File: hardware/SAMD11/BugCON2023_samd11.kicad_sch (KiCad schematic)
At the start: 30 parts, among them J1 I2C, J3 PAD2, J4 PAD, J5 Serial, P1 USB_C_Plug_USB2.0, Q1 DMG3415U-7, SW1 SW_Push, SW2 ON, U1 ATSAMD11C14A-SS, U2 AP2112K-3.3

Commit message: change MCU for RP2040
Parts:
- removed SW1: SW_Push, Button_Switch_SMD:SW_SPST_TL3342, symbol Switch:SW_Push
- removed U1: ATSAMD11C14A-SS, Package_SO:SOIC-14_3.9x8.7mm_P1.27mm, symbol MCU_Microchip_SAMD:ATSAMD11C14A-SS
- added C10, C12, C14, C15, C16, C17, C18, C19, C20: 0.1uF, Capacitor_SMD:C_0402_1005Metric, symbol Device:C_Small
- added C11, C9: 27pF, Capacitor_SMD:C_0402_1005Metric, symbol Device:C_Small
- added C13, C8: 1uF, Capacitor_SMD:C_0402_1005Metric, symbol Device:C_Small
- added JP1: BOOT, Jumper:SolderJumper-2_P1.3mm_Open_TrianglePad1.0x1.5mm, symbol Jumper:Jumper_2_Open
- added R10: 10k, Resistor_SMD:R_0402_1005Metric, symbol Device:R_Small
- added R7, R8: 27, Resistor_SMD:R_0402_1005Metric, symbol Device:R_Small
- added R9: 1k, Resistor_SMD:R_0402_1005Metric, symbol Device:R_Small
- added RESET1: SW, CatSniffer:TS1088R02026, symbol CatSniffer-rescue:SW_Push-Switch-CatStick-rescue-CatSniffer-rescue
- added U1: W25Q16JV, CatSniffer:W25Q16JVUUIQ, symbol Memory_Flash:W25Q128JVS
- added U3: RP2040, Package_DFN_QFN:QFN-56-1EP_7x7mm_P0.4mm_EP3.2x3.2mm, symbol MCU_RaspberryPi:RP2040
- added Y1: 12MHz, Crystal:Crystal_SMD_3225-4Pin_3.2x2.5mm, symbol Device:Crystal_GND23_Small
- C1: value 100nF -> 0.1uF; footprint Capacitor_SMD:C_0603_1608Metric -> Capacitor_SMD:C_0402_1005Metric; LCSC# C1591 -> (none); Mouser# (none) -> 963-MSAST105SB7104KF; Proveedor LCSC -> (none); manf# CL10B104KB8NNNC -> MSAST105SB7104KFNB25; provedor (none) -> Mouser
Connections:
- net +3.3V: now also C13.1, C14.1, C15.1, C16.1, C17.1, C18.1, C19.1, C20.1, R10.1, U1.8 (VCC), U3.1 (IOVDD), U3.10 (IOVDD), U3.22 (IOVDD), U3.33 (IOVDD), U3.42 (IOVDD), U3.43 (ADC_AVDD), U3.44 (VREG_IN), U3.48 (USB_VDD), U3.49 (IOVDD)
- net D+: now also R7.1
- net D-: now also R8.1
- net GND: now also C10.2, C11.2, C12.2, C13.2, C14.2, C15.2, C16.2, C17.2, C18.2, C19.2, C20.2, C8.2, C9.2, JP1.1 (A), RESET1.2, U1.4 (GND), U3.19 (TESTEN), U3.57 (GND), Y1.2, Y1.4
- net PIN: now also U3.35 (GPIO23)
- net RX: now also U3.12 (GPIO9)
- net SCL: now also U3.16 (GPIO13)
- net SDA: now also U3.15 (GPIO12)
- net TX: now also U3.11 (GPIO8)
- new net: C9.1, U3.20 (XIN), Y1.1
- new net: R9.2, U3.21 (XOUT)
- new net: R8.2, U3.46 (USB_DM)
- new net: R7.2, U3.47 (USB_DP)
- new net: C11.1, R9.1, Y1.3
- new net +1V2: C10.1, C12.1, C8.1, U3.23 (DVDD), U3.45 (VREG_VOUT), U3.50 (DVDD)
- new net QSPI_CS: JP1.2 (B)
- new net QSPI_SCK: U1.6 (CLK), U3.52 (QSPI_SCLK)
- new net QSPI_SD0: U1.5 (DI(IO0)), U3.53 (QSPI_SD0)
- new net QSPI_SD1: U1.2 (DO(IO1)), U3.55 (QSPI_SD1)
- new net QSPI_SD2: U1.3 (IO2), U3.54 (QSPI_SD2)
- new net QSPI_SD3: U1.7 (IO3), U3.51 (QSPI_SD3)
- new net QSPI_SS: R10.2, U1.1 (~{CS}), U3.56 (QSPI_SS)
- new net RESET: RESET1.1, U3.26 (RUN)
- no-connect marks 1 -> 28
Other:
- note added: "FLASH"
- note added: "MICROCONTROLLER"
- note removed: "Microcontroller"
- note removed: "RST"
- moved on the sheet: C4, C5, C6, C7, D2, D3, D4, D5, J3, J4, R4

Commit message: upd floorplan on rp2040 badge
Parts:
- RESET1: footprint CatSniffer:TS1088R02026 -> Button_Switch_SMD:SW_SPST_TL3342; LCSC# C455281 -> (none); manf# TS-1088R-02526 -> (none)
- U1: footprint CatSniffer:W25Q16JVUUIQ -> BugCON2023_samd11:W25Q16JVUUIQ
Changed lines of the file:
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@@
       (effects (font (size 1.27 1.27)))
     )
-    (property "Footprint" "CatSniffer:TS1088R02026" (at 188.468 147.955 0)
+    (property "Footprint" "Button_Switch_SMD:SW_SPST_TL3342" (at 188.468 147.955 0)
       (effects (font (size 1.27 1.27)) hide)
     )
@@
       (effects (font (size 1.27 1.27)) hide)
     )
-    (property "LCSC#" "C455281" (at 188.468 153.035 0)
+    (property "LCSC#" "" (at 188.468 153.035 0)
       (effects (font (size 1.27 1.27)) hide)
     )
-    (property "manf#" "TS-1088R-02526" (at 188.468 153.035 0)
+    (property "manf#" "" (at 188.468 153.035 0)
       (effects (font (size 1.27 1.27)) hide)
     )
@@
       (effects (font (size 1.27 1.27)) (justify left))
     )
-    (property "Footprint" "CatSniffer:W25Q16JVUUIQ" (at 81.661 252.603 0)
+    (property "Footprint" "BugCON2023_samd11:W25Q16JVUUIQ" (at 81.661 252.603 0)
       (effects (font (size 1.27 1.27)) hide)
     )

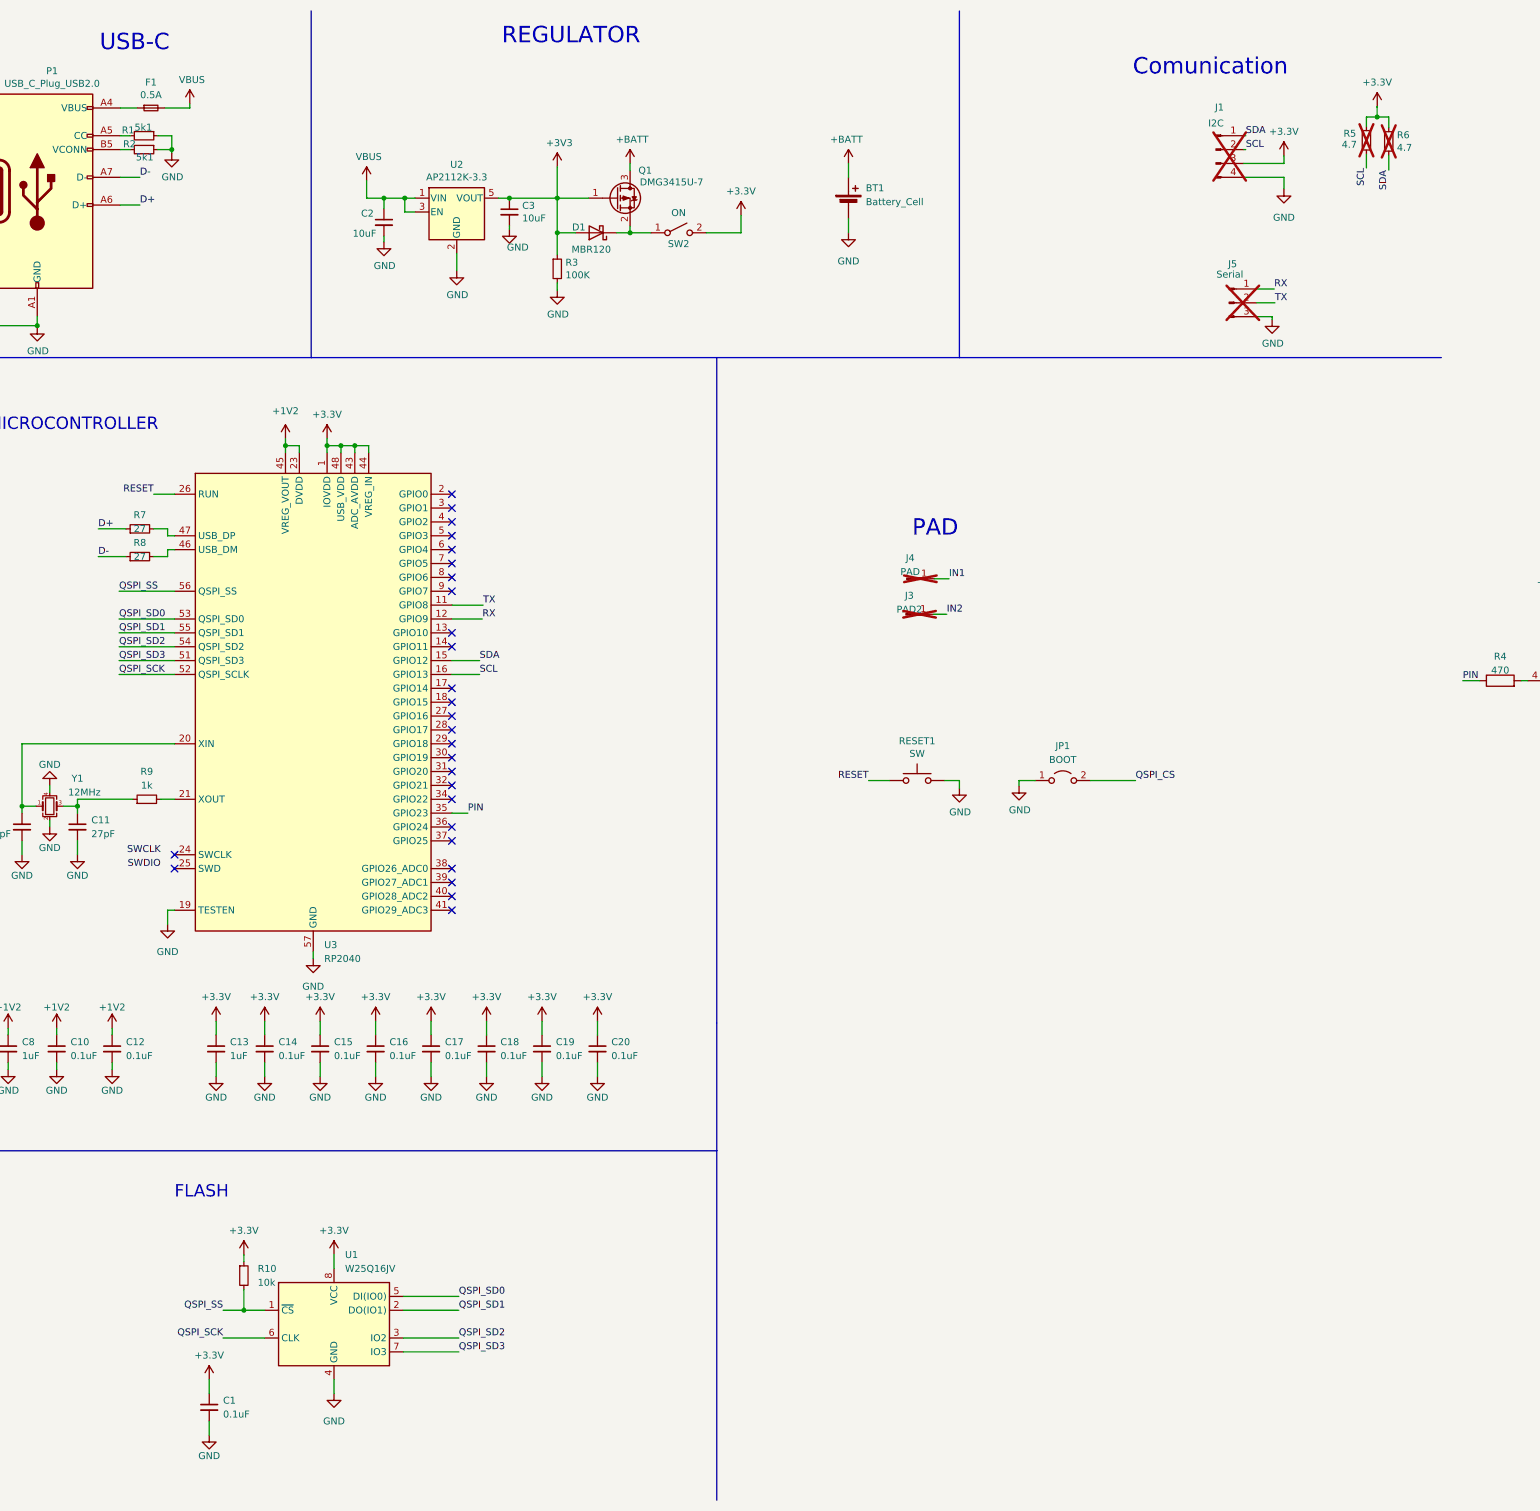
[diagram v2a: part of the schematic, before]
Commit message: Start new routing RP2040
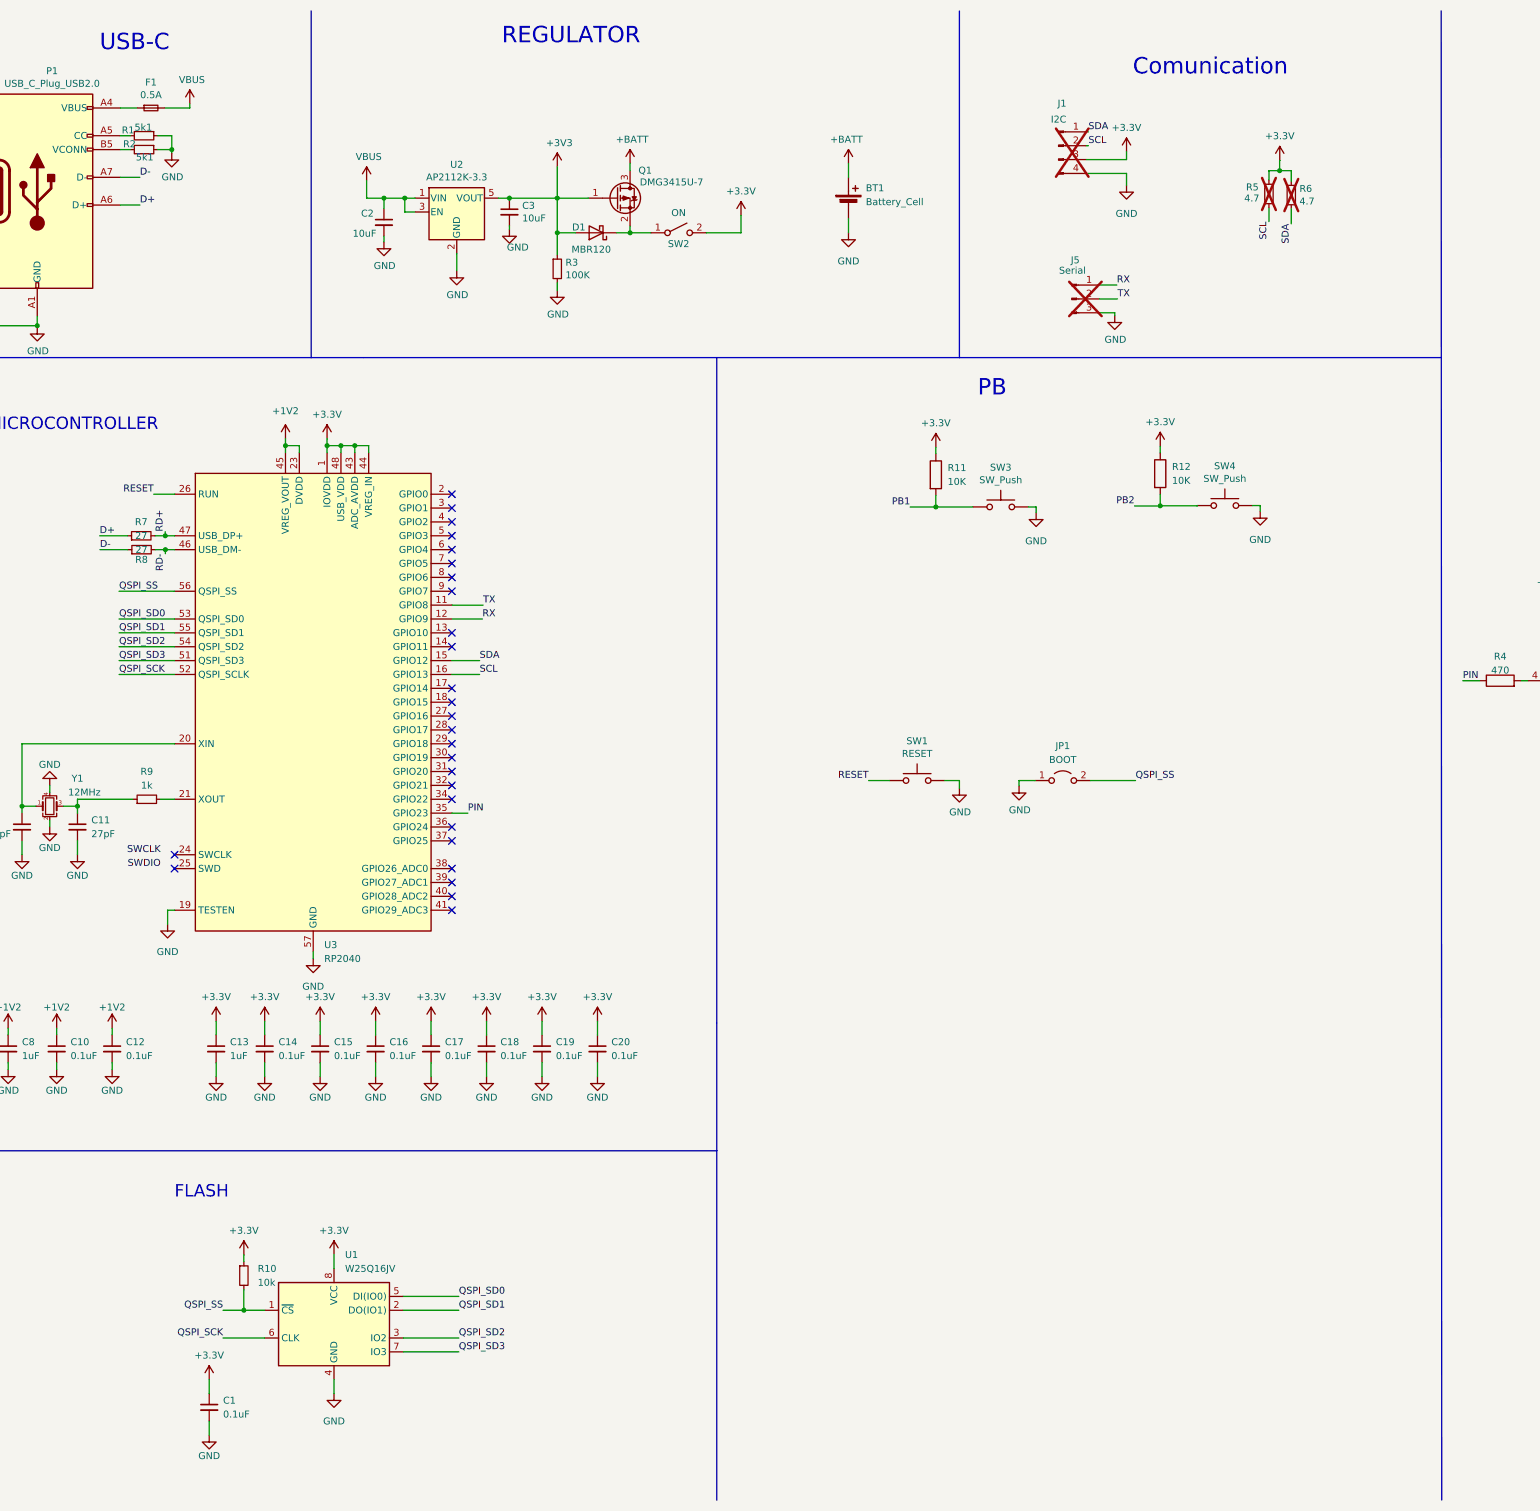
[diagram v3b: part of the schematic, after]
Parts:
- removed J3: PAD2, BugCON2023_samd11:Piad, symbol Connector:Conn_01x01_Pin
- removed J4: PAD, BugCON2023_samd11:Piad, symbol Connector:Conn_01x01_Pin
- added R11, R12: 10K, Resistor_SMD:R_0603_1608Metric, symbol Device:R
- added SW3, SW4: SW_Push, Button_Switch_SMD:SW_SPST_TL3342, symbol CatSniffer-rescue:SW_Push-Switch-CatStick-rescue-CatSniffer-rescue
- SW1: renamed from RESET1; value SW -> RESET
- U1: footprint BugCON2023_samd11:W25Q16JVUUIQ -> BugCON2023_samd11:W25Q16JVUXIQ_WIN
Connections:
- net QSPI_CS is gone; now on net QSPI_SS: JP1.2 (B)
- net +3.3V: now also R11.1, R12.1
- net GND: now also SW3.2, SW4.2
- net RD-: now reaches R8.2, U3.46 (USB_DM-)
- net RD+: now reaches R7.2, U3.47 (USB_DP+)
- new net PB1: R11.2, SW3.1
- new net PB2: R12.2, SW4.1
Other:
- note added: "PB"
- note removed: "PAD"
- moved on the sheet: J1, J5, R5, R6, R7, R8

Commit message: Update routing RP2040
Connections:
- net PB1: now also U3.39 (GPIO27_ADC1)
- net PB2: now also U3.37 (GPIO25)
- no-connect marks 28 -> 26
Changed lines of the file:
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@@
   (no_connect (at 103.251 169.164))
   (no_connect (at 103.251 118.364))
-  (no_connect (at 103.251 171.704))
   (no_connect (at 52.451 166.624))
   (no_connect (at 103.251 153.924))
@@
   (no_connect (at 103.251 100.584))
   (no_connect (at 103.251 136.144))
-  (no_connect (at 103.251 164.084))
   (no_connect (at 103.251 105.664))
   (no_connect (at 103.251 174.244))
@@
     (stroke (width 0) (type default))
   )
+  (wire (pts (xy 106.172 164.084) (xy 103.251 164.084))
+    (stroke (width 0) (type default))
+  )
   (wire (pts (xy 24.511 164.084) (xy 24.511 166.624))
     (stroke (width 0) (type default))
@@
   )
   (wire (pts (xy 19.685 69.723) (xy 27.305 69.723))
+    (stroke (width 0) (type default))
+  )
+  (wire (pts (xy 105.6132 171.704) (xy 103.251 171.704))
     (stroke (width 0) (type default))
   )
@@
     (effects (font (size 1.27 1.27)) (justify right bottom))
   )
+  (label "PB2" (at 106.172 164.084 0) (fields_autoplaced)
+    (effects (font (size 1.27 1.27)) (justify left bottom))
+  )
   (label "QSPI_SS" (at 61.341 250.063 180) (fields_autoplaced)
     (effects (font (size 1.27 1.27)) (justify right bottom))
@@
     (effects (font (size 1.27 1.27)) (justify left bottom))
   )
+  (label "PB1" (at 105.6132 171.704 0) (fields_autoplaced)
+    (effects (font (size 1.27 1.27)) (justify left bottom))
+  )

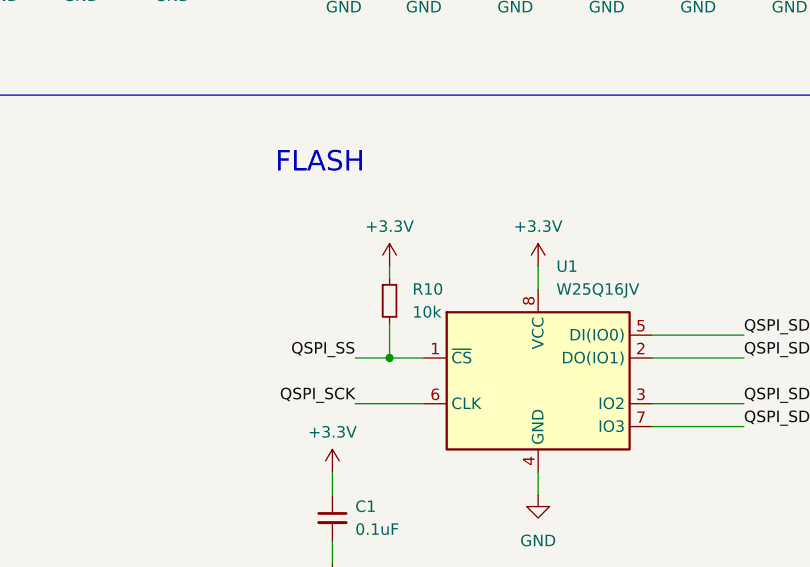
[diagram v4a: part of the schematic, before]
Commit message: upd BOM and upd silkscreen on RP2040
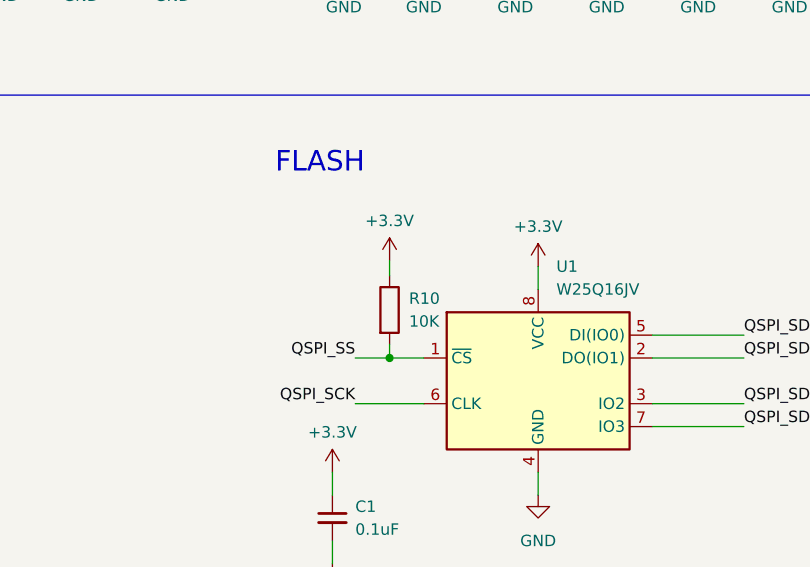
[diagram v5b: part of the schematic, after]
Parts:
- removed R10: 10k, Resistor_SMD:R_0402_1005Metric, symbol Device:R_Small
- added R10: 10K, Resistor_SMD:R_0603_1608Metric, symbol Device:R
- C1, C10, C12, C14, C15, C16, C17, C18, C19, C20: Mouser# 963-MSAST105SB7104KF -> (none); Proveedor (none) -> MOUSER; provedor Mouser -> (none)
- C11, C9: LCSC# (none) -> C88883; Mouser# 81-GJM1555C1H270FB1D -> (none); Proveedor (none) -> LCSC; provedor Mouser -> (none)
- C13, C8: LCSC# (none) -> C14445; Mouser# 963-MSRLJ103SB5105MF -> (none); Proveedor (none) -> LCSC; manf# MSRLJ103SB5105MFNA01 -> CL05A105KP5NNNC; provedor Mouser -> (none)
- F1: LCSC# (none) -> C2649565
- R11, R12: LCSC# (none) -> C98220; Proveedor (none) -> LCSC; manf# (none) -> RC0603FR-0710KL
- R7, R8: Mouser# 755-ESR01MZPF27R0 -> (none); Proveedor (none) -> MOUSER; provedor Mouser -> (none)
- R9: LCSC# (none) -> C852624; Mouser# 594-MCS0402MD1001DE0 -> (none); Proveedor (none) -> LCSC; manf# MCS0402MD1001DE000 -> RT0402BRD071KL; provedor Mouser -> (none)
- SW1, SW3, SW4: LCSC# (none) -> C318889; Proveedor (none) -> LCSC; manf# (none) -> TS-1187A-C-C-B; provedor LCSC -> (none)
- U1: LCSC# (none) -> C2843335; Mouser# 454-W25Q16JVUUIQTR -> (none); Proveedor (none) -> LCSC; manf# W25Q16JVUUIQ TR -> W25Q16JVUXIQ; provedor Mouser -> (none)
- U3, Y1: Proveedor (none) -> LCSC; provedor LCSC -> (none)
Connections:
- net +3.3V: now also R10.1
- net QSPI_SS: now also R10.2
